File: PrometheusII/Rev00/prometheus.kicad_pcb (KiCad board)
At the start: 4 copper layers, 223.5 x 222.3 mm, 194 parts, among them J1 0878311420, J10 Conn_02x02_Odd_Even, J11 Conn_02x02_Odd_Even, J16 Conn_02x07_Odd_Even, J17 Conn_02x07_Odd_Even, J18 Conn_02x07_Odd_Even, J19 Conn_02x07_Odd_Even, J2 Conn_02x08_Odd_Even, J3 Conn_02x02_Odd_Even, J4 Conn_02x02_Odd_Even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

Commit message: most power supply routing
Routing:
- net +3V3: track 80.0 -> 262.7 mm, vias 0 -> 6
- net -12V: track 37.6 -> 156.6 mm, vias 6 -> 7
- net +12V: track 32.3 -> 109.1 mm
- net /CLK1_T: track 0.00 -> 54.2 mm, vias 0 -> 2
- net +5V: track 6.44 -> 60.2 mm
- net GND: track 788.1 -> 751.1 mm, vias 10 -> 23
- net /TAP0: track 0.00 -> 30.8 mm, vias 0 -> 2
- net /TAP1: track 0.00 -> 28.6 mm, vias 0 -> 2
- net /TAP3: track 0.00 -> 28.5 mm, vias 0 -> 2
- net /TAP10: track 1.79 -> 29.6 mm
- net /TAP2: track 0.00 -> 27.4 mm, vias 0 -> 2
- net /TAP9: track 2.28 -> 28.9 mm, vias 1 -> 3
- net Net-(Q1-Pad3): track 0.00 -> 26.1 mm
- net /TAP4: track 2.45 -> 28.2 mm, vias 1 -> 2
- net /EXT_CLK: track 0.00 -> 24.2 mm
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
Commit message: checkpoint
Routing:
- net /CV_FILT: track 1.29 -> 126.5 mm
- net GND: track 751.1 -> 648.2 mm
- net /GLITCH_IN_T: track 1.91 -> 84.8 mm
- net /LFSR1_IN: track 0.00 -> 41.1 mm, vias 0 -> 2
- net /TAP8: track 5.26 -> 44.3 mm, vias 1 -> 3
- net /EXT_CLK_EN_T: track 7.74 -> 44.0 mm, vias 0 -> 2
- net /LFSR0_IN: track 0.00 -> 32.9 mm, vias 0 -> 2
- net /JTAG_TDI: track 1.76 -> 30.6 mm, vias 0 -> 1
- net /TAP11: track 16.6 -> 41.3 mm, vias 2 -> 3
- net /JTAG_TDO: track 0.00 -> 21.0 mm, vias 0 -> 1
- net /TAP5: track 14.4 -> 31.3 mm, vias 0 -> 2
- net /OUT: track 1.98 -> 17.8 mm, vias 0 -> 1
- net /TAP9: track 28.9 -> 43.1 mm
- net /TAP6: track 10.7 -> 24.6 mm, vias 1 -> 2
- net /TAP7: track 20.5 -> 31.8 mm, vias 0 -> 2
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
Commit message: first pass main board layout
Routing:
- net GND: track 648.2 -> 321.6 mm, vias 23 -> 91
- net /JTAG_TCK: track 0.00 -> 44.9 mm, vias 0 -> 2
- net /JTAG_TMS: track 0.80 -> 45.3 mm, vias 0 -> 2
- net +3V3: track 262.7 -> 292.8 mm
- net /VJTAG: track 0.00 -> 25.8 mm, vias 0 -> 2
- net +1V8: track 11.5 -> 26.0 mm
- net +12V: track 109.1 -> 115.1 mm, vias 6 -> 7
- net -12V: track 156.6 -> 162.5 mm
- net /TAP8: track 44.3 -> 39.2 mm
- net /CLK1_T: track 54.2 -> 59.4 mm
- net /LFSR1_IN: track 41.1 -> 45.4 mm
- net /TAP5: track 31.3 -> 27.7 mm
- net /TAP4: track 28.2 -> 30.8 mm
- net /TAP9: track 43.1 -> 41.2 mm
- net /JTAG_TDO: track 21.0 -> 22.7 mm
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- added copper zone on F.Cu, net +12V
- added copper zone on F.Cu, net -12V
- added copper zone on In2.Cu, net GND

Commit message: checkpoint
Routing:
- net GND: track 321.6 -> 693.9 mm, vias 91 -> 92
- net /VOCT_CV_P: track 0.00 -> 74.2 mm, vias 0 -> 1
- net /VOCT_ATV_P: track 0.00 -> 61.4 mm
- net /VOCT_FINE_P: track 0.00 -> 42.8 mm
- net /CV_FILT_P: track 0.00 -> 34.6 mm
- net /LFO_P: track 0.00 -> 23.2 mm
- net /VOCT_SEMI_P: track 0.00 -> 19.2 mm
- net Net-(C41-Pad1): track 0.00 -> 16.7 mm
- net Net-(R53-Pad1): track 0.00 -> 12.5 mm
- net /EXT_CLK_SW_P: track 0.00 -> 10.7 mm
- net Net-(D4-Pad1): track 0.00 -> 10.1 mm
- net /EXT_CLK_P: track 0.00 -> 9.50 mm
- net /FREQ_LOCK_P: track 0.00 -> 9.33 mm
- net Net-(D11-Pad1): track 0.00 -> 8.29 mm
- net +3V3: track 292.8 -> 299.2 mm
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
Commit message: checkpoint
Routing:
- net +3V3: track 299.2 -> 607.3 mm, vias 6 -> 10
- net GND: track 693.9 -> 929.8 mm, vias 92 -> 98
- net /PARAM_0_CV_P: track 2.16 -> 92.3 mm
- net /PARAM_0_P: track 0.00 -> 70.5 mm
- net Net-(C41-Pad1): track 16.7 -> 36.2 mm, vias 0 -> 3
- net /CV_FILT_P: track 34.6 -> 31.5 mm, vias 0 -> 1
- net /VOCT_ATV_P: track 61.4 -> 58.7 mm
- net /VOCT_FINE_P: track 42.8 -> 41.4 mm
- net /VOCT_CV_P: track 74.2 -> 72.8 mm
- net Net-(Q6-Pad1): track 2.92 -> 2.38 mm

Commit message: checkpoint
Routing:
- net GND: track 929.8 -> 978.9 mm, vias 98 -> 102
- net +3V3: track 607.3 -> 616.9 mm

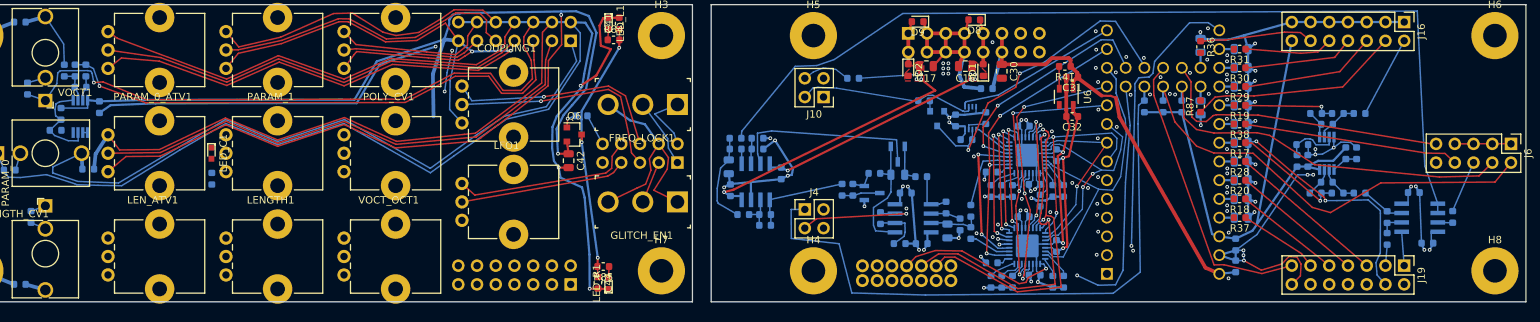
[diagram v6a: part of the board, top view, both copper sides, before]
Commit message: CIB signal routing finished
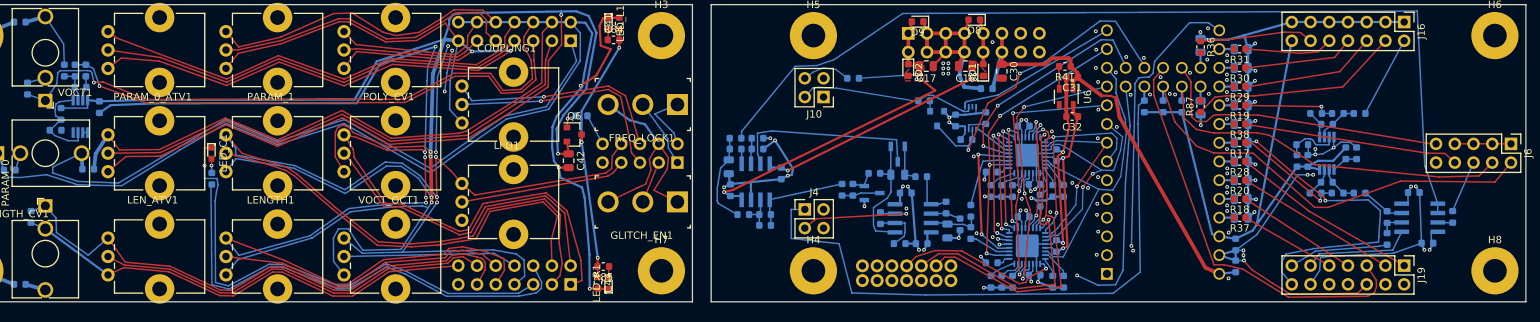
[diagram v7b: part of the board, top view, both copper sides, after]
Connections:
- C12 pad 1: /LEN_KNOB_T -> /VOCT_OCT_T
- C26 pad 1: /VOCT_OCT_T -> /LEN_KNOB_T
- J18 pad 12: /VOCT_OCT_P -> /LEN_ATV_P
- J18 pad 14: /TAPS_LED_P -> /LEN_CV_P
- J18 pad 2: /LEN_ATV_P -> /POLY_P
- J18 pad 4: /LEN_CV_P -> /PARAM_1_P
- J18 pad 6: /POLY_P -> /TAPS_LED_P
- J18 pad 8: /PARAM_1_P -> /VOCT_OCT_P
- J19 pad 1: /LEN_ATV -> /POLY
- J19 pad 11: /VOCT_OCT -> /LEN_ATV
- J19 pad 13: /TAPS_LED_T -> /_LEN_CV
- J19 pad 3: /_LEN_CV -> /PARAM_1
- J19 pad 5: /POLY -> /TAPS_LED_T
- J19 pad 7: /PARAM_1 -> /VOCT_OCT
- R18 pad 1: /LEN_KNOB -> /VOCT_OCT
- R18 pad 2: /LEN_KNOB_T -> /VOCT_OCT_T
- R37 pad 1: /VOCT_OCT -> /LEN_KNOB
- R37 pad 2: /VOCT_OCT_T -> /LEN_KNOB_T
- U1 pad 29: /LEN_KNOB_T -> /VOCT_OCT_T
- U1 pad 30: /VOCT_OCT_T -> /LEN_KNOB_T
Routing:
- net GND: track 978.9 -> 1474.7 mm, vias 102 -> 112
- net +3V3: track 616.9 -> 736.9 mm, vias 10 -> 14
- net /TAPS_LED_P: track 0.00 -> 64.9 mm
- net /LEN_CV_P: track 2.10 -> 63.8 mm
- net /PARAM_1_P: track 0.00 -> 59.0 mm
- net /LEN_ATV_P: track 0.00 -> 54.4 mm
- net /POLY_P: track 0.00 -> 44.7 mm
- net /LEN_KNOB_P: track 0.00 -> 39.4 mm
- net /VOCT_OCT_P: track 0.00 -> 23.6 mm
- net /TAPS_LED_T: track 39.4 -> 55.7 mm
- net /_LEN_CV: track 2.86 -> 13.5 mm
- net /LEN_ATV: track 4.58 -> 14.7 mm
- net /VOCT_OCT: track 11.0 -> 16.6 mm
- net /PARAM_1: track 18.1 -> 22.2 mm
- net /POLY: track 21.8 -> 25.8 mm
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
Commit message: CIB ground pours
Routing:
- net +3V3: track 736.9 -> 742.0 mm
- net GND: track 1474.7 -> 1476.2 mm
- added copper zone on B.Cu, net GND
- added copper zone on F.Cu, net GND
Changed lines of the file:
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@@
     (thickness 1.6)
     (drawings 40)
-    (tracks 1616)
+    (tracks 1620)
     (zones 0)
     (modules 194)
@@
     (user_trace_width 0.508)
     (trace_clearance 0.1524)
-    (zone_clearance 0.2)
+    (zone_clearance 0.152)
     (zone_45_only no)
     (trace_min 0.15)
@@
   (segment (start 90.3235 108.726) (end 85.679079 108.840421) (width 0.2) (layer F.Cu) (net 1))
   (segment (start 79.75 106.72) (end 81.4335 107.066) (width 0.2) (layer F.Cu) (net 1))
-  (segment (start 94.2935 111.666) (end 95.746 113.324) (width 0.2) (layer F.Cu) (net 1))
   (via (at 92.2135 109.726) (size 0.508) (drill 0.254) (layers F.Cu B.Cu) (net 1))
-  (segment (start 92.2135 109.726) (end 94.2935 111.666) (width 0.2) (layer F.Cu) (net 1))
   (segment (start 112.0335 126.486) (end 110.49 127.01) (width 0.2) (layer F.Cu) (net 1))
   (segment (start 111.8835 123.776) (end 112.0335 126.486) (width 0.2) (layer F.Cu) (net 1))
@@
   (segment (start 90.8735 115.926) (end 86.2935 116.066) (width 0.2) (layer B.Cu) (net 1))
   (segment (start 86.2935 116.066) (end 80.3735 116.726) (width 0.2) (layer B.Cu) (net 1))
+  (segment (start 43.0275 106.419) (end 41.4275 106.1085) (width 0.3) (layer B.Cu) (net 1))
+  (segment (start 95.746 113.324) (end 93.7235 116.176) (width 0.2) (layer F.Cu) (net 1))
+  (segment (start 93.7235 116.176) (end 92.3635 115.906) (width 0.2) (layer F.Cu) (net 1))
   (via (at 155.5495 113.7158) (size 0.508) (drill 0.254) (layers F.Cu B.Cu) (net 2))
   (via (at 139.9285 111.5695) (size 0.508) (drill 0.254) (layers F.Cu B.Cu) (net 2))
@@
   (segment (start 80.6435 117.166) (end 86.3035 116.486) (width 0.2) (layer B.Cu) (net 7))
   (segment (start 86.3035 116.486) (end 90.3635 116.366) (width 0.2) (layer B.Cu) (net 7))
+  (segment (start 91.6335 115.886) (end 91.9435 116.416) (width 0.2) (layer F.Cu) (net 7))
+  (segment (start 91.9435 116.416) (end 94.1135 116.616) (width 0.2) (layer F.Cu) (net 7))
+  (segment (start 94.1135 116.616) (end 95.746 118.324) (width 0.2) (layer F.Cu) (net 7))
   (segment (start 200.6727 125.3491) (end 198.4502 125.5776) (width 0.3) (layer B.Cu) (net 8))
   (segment (start 168.948 97.17) (end 168.9735 95.504) (width 0.508) (layer F.Cu) (net 8))
@@
       )
     )
+  )
+  (zone (net 1) (net_name GND) (layer B.Cu) (hatch edge 0.508)
+    (connect_pads (clearance 0.152))
+    (min_thickness 0.152)
+    (fill yes (arc_segments 32) (thermal_gap 0.508) (thermal_bridge_width 0.508))
+    (polygon
+      (pts
+        (xy 17.0135 89.576) (xy 126.4935 89.576) (xy 126.4935 128.866) (xy 17.0135 128.866)
+      )
+    )
+  )
+  (zone (net 1) (net_name GND) (layer F.Cu) (hatch edge 0.508)
+    (connect_pads (clearance 0.152))
+    (min_thickness 0.152)
+    (fill yes (arc_segments 32) (thermal_gap 0.508) (thermal_bridge_width 0.508))
+    (polygon
+      (pts
+        (xy 17.0135 89.576) (xy 126.4935 89.576) (xy 126.4935 128.866) (xy 17.0135 128.866)
+      )
+    )
